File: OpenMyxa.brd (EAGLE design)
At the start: 56 x 56 mm, 107 parts, among them CON1 USB, CON2 PINHEAD_1X01-2, CON3 CON-4P-STRAIGHT, CON4 CON-4P-STRAIGHT, CON5 CON-4P-STRAIGHT, CON6 CON-4P-STRAIGHT, CON7 CON-4P-STRAIGHT, CON8 CON-6P, CON9 PINHEAD_1X01-2, IC1 TPD3S014DBVR-SOT23-6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

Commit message: V0.2 import
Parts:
- removed D3: TPSMC62A, TVS_diodes:DO-214AB(SMC)
- removed MODULE1: MITOHONDRIQUE, mitohondrique:MITOHONDRIQUE
- added MODULE2: MITOHONDRIQUE-TH, zubax_modules:MITOHONDRIQUE
- CON3, CON4, CON5, CON6: device myxa_masterlib:JST_GH-4P-STRAIGHT -> Connectors:JST_GH-4P-STRAIGHT
- moved R7 12.3 mm to (-21.2, 5.90)
- moved PAD6 7.30 mm to (-26.5, -3.65), turned to 270 degrees
- moved PAD7 7.30 mm to (-26.5, 3.65), turned to 270 degrees
- moved U$13 4.69 mm to (-9.28, 18.1)
- moved R10 4.10 mm to (-3.00, 1.25), turned to 90 degrees
- moved LED5 3.76 mm to (-13.3, 18.5), turned to 90 degrees
- moved LED4 3.73 mm to (-10.3, 18.5), turned to 270 degrees
- moved LED3 2.90 mm to (-7.28, 18.5), turned to 270 degrees
- moved R13 2.57 mm to (-9.35, 16.8), flipped to the top
- moved R12 2.30 mm to (-8.30, 16.8), flipped to the top
- moved R11 2.19 mm to (-7.25, 16.8), flipped to the top
- moved CON2 2.00 mm to (-26.5, 1.00), turned to 270 degrees
- moved CON9 2.00 mm to (-26.5, -1.00), turned to 270 degrees
- moved R28 1.67 mm to (-10.2, 22.4)
- moved D7 1.36 mm to (-11.1, 16.5), flipped to the top, turned to 90 degrees
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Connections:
- removed net N$23: CON3.2, CON4.2, IC3.6
- removed net N$24: CON7.2, R25.2
- removed net N$35: CON3.3, CON4.3, IC3.7
- new net LED_BLUE: MODULE2.32, R11.2
- new net N$21: CON3.2, CON4.2, IC3.7
- new net N$22: CON3.3, CON4.3, IC3.6
- net BEC_ENABLE_OUT: now also MODULE2.24; no longer MODULE1.24
- net CAN1_LED: now also MODULE2.36; no longer MODULE1.27
- net CAN1_RX: now also MODULE2.41; no longer MODULE1.41
- net CAN1_TX: now also MODULE2.42; no longer MODULE1.42
- net CAN1_VDD: now also CON3.1, CON4.1; no longer CON3.4, CON4.4
- net CAN2_LED: now also MODULE2.37; no longer MODULE1.26
- net CAN2_RX: now also MODULE2.39; no longer MODULE1.39
- net CAN2_TX: now also MODULE2.40; no longer MODULE1.40
- net CAN2_VDD: now also CON5.1, CON6.1; no longer CON5.4, CON6.4
- net GAIN_OUT: now also MODULE2.25; no longer MODULE1.38
- net GATE_ENABLE_OUT: now also MODULE2.26; no longer MODULE1.37
- net GND: now also CON7.4, MODULE2.2; no longer CON7.1, MODULE1.2
- net GNDD: now also CON3.4, CON4.4, CON5.4, CON6.4; no longer CON3.1, CON4.1, CON5.1, CON6.1
- net GPIO1: now also MODULE2.28; no longer MODULE1.35
- net GPIO2: now also MODULE2.27; no longer MODULE1.36
- net LED_GREEN: now also MODULE2.31; no longer MODULE1.32
- net LED_RED: now also MODULE2.30; no longer MODULE1.33
- net N$18: now also MODULE2.29; no longer MODULE1.34
- net N$19: now also CON7.2, R8.2; no longer CON7.4, F1.P$1
- net N$20: now also R25.2; no longer R8.2
- net N$44: now also CON5.3, CON6.3; no longer CON5.2, CON6.2
- net N$46: now also CON5.2, CON6.2; no longer CON5.3, CON6.3
- net N$5: now also MODULE2.33; no longer MODULE1.30
- net N$51: now also MODULE2.34; no longer MODULE1.29
- net N$55: now also MODULE2.35; no longer MODULE1.28
- net N$6: now also CON7.1, F1.P$1; no longer MODULE1.31, R11.2
- net PGND: no longer D3.A
- net PHASE_A: now also MODULE2.5; no longer MODULE1.5
- net PHASE_A_CURRENT_SHUNT_N: now also MODULE2.16; no longer MODULE1.16
- net PHASE_A_CURRENT_SHUNT_P: now also MODULE2.17; no longer MODULE1.17
- net PHASE_A_GATE_HIGH: now also MODULE2.4; no longer MODULE1.4
- net PHASE_A_GATE_LOW: now also MODULE2.6; no longer MODULE1.6
- net PHASE_A_GND: now also MODULE2.7; no longer MODULE1.7
- net PHASE_B: now also MODULE2.9; no longer MODULE1.9
- net PHASE_B_CURRENT_SHUNT_N: now also MODULE2.18; no longer MODULE1.18
- net PHASE_B_CURRENT_SHUNT_P: now also MODULE2.19; no longer MODULE1.19
- net PHASE_B_GATE_HIGH: now also MODULE2.8; no longer MODULE1.8
- net PHASE_B_GATE_LOW: now also MODULE2.10; no longer MODULE1.10
- net PHASE_B_GND: now also MODULE2.11; no longer MODULE1.11
- net PHASE_C: now also MODULE2.13; no longer MODULE1.13
- net PHASE_C_GATE_HIGH: now also MODULE2.12; no longer MODULE1.12
- net PHASE_C_GATE_LOW: now also MODULE2.14; no longer MODULE1.14
- net PHASE_C_GND: now also MODULE2.15; no longer MODULE1.15
- net TEMPERATURE_SENSOR: now also MODULE2.20; no longer MODULE1.20
- net UART_RX: now also MODULE2.23, R29.2; no longer MODULE1.23, R28.2
- net UART_TX: now also MODULE2.22, R28.2; no longer MODULE1.22, R29.2
- net VDC: now also MODULE2.3; no longer D3.C, MODULE1.3
- net VDD_5V: now also MODULE2.1; no longer MODULE1.1
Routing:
- net GAIN_OUT: track 46.1 -> 15.0 mm
- net LED_BLUE: track 0.00 -> 28.4 mm
- net GATE_ENABLE_OUT: track 45.4 -> 18.6 mm
- net N$6: track 30.7 -> 5.93 mm, vias 1 -> 0
- net GPIO2: track 41.8 -> 17.4 mm
- net GPIO1: track 45.7 -> 29.2 mm
- net CAN1_LED: track 25.5 -> 37.0 mm, vias 0 -> 1
- net N$23: track 11.5 -> 0.00 mm
- net N$22: track 0.00 -> 11.5 mm
- net CAN2_LED: track 39.0 -> 27.8 mm, vias 2 -> 1
- net N$35: track 10.4 -> 0.00 mm
- net N$21: track 0.00 -> 10.4 mm
- net N$55: track 9.44 -> 19.1 mm, vias 0 -> 1
- net LED_RED: track 32.3 -> 23.7 mm, vias 1 -> 0
- net N$5: track 2.09 -> 9.95 mm
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- added copper zone on layer 15, net VDD_5V
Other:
- outline, holes or cut-outs redrawn
- board text added: "OpenMyxa0.2"
- board text removed: "OpenMyxa"

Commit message: minor updates
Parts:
- moved CON2 1.00 mm to (-25.5, 1.00)
- moved CON9 1.00 mm to (-25.5, -1.00)
- moved PAD6 1.00 mm to (-25.5, -3.65)
- moved PAD7 1.00 mm to (-25.5, 3.65)
- moved C32 0.80 mm to (14.2, 21.4)
- moved C35 0.80 mm to (14.2, -21.4)
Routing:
- net GND: track 30.7 -> 33.5 mm

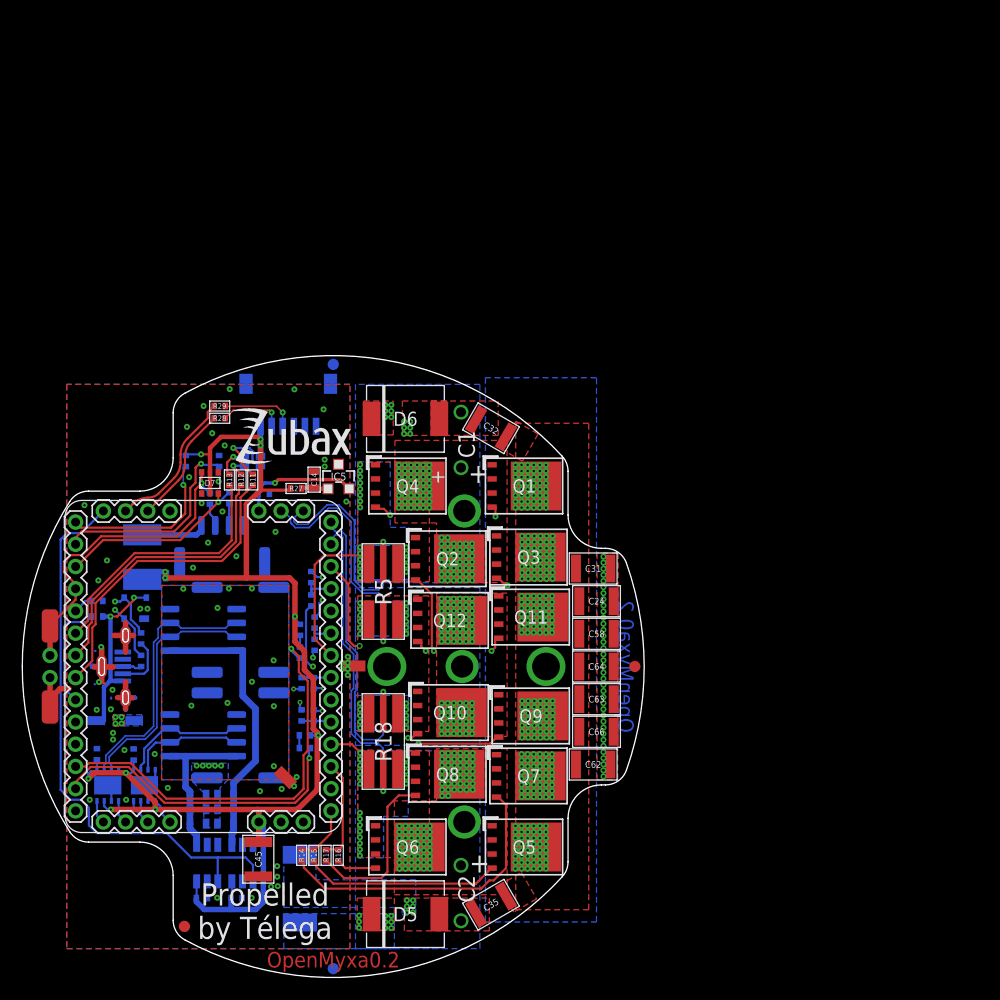
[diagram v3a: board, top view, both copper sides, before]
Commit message: Connectors color fix
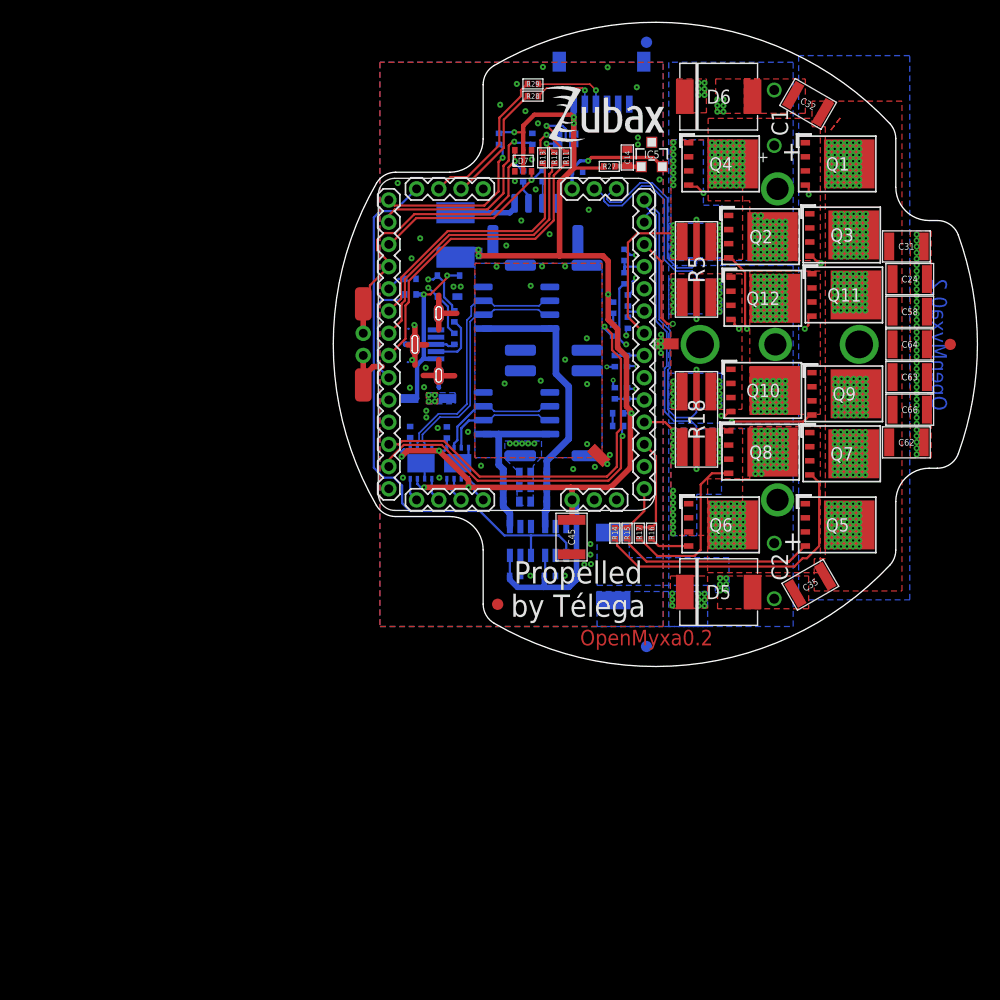
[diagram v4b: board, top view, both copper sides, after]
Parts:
- CON3, CON4, CON5, CON6, CON7: value CON-4P-STRAIGHT -> CON-4P-TABS-STRAIGHT
- MODULE2: device zubax_modules:MITOHONDRIQUE -> zubax_modules:MITOHONDRIQUE-TH
- moved C32 40.8 mm to (42.8, 50.6)
- moved C35 40.7 mm to (43.0, 7.35)
- moved U$5 40.6 mm to (55.5, 29.0)
- moved C1 40.5 mm to (39.2, 49.4)
- moved C12 40.5 mm to (10.2, 21.1)
- moved C13 40.5 mm to (21.9, 44.5)
- moved C14 40.5 mm to (26.5, 45.8)
- moved C2 40.5 mm to (39.2, 8.60)
- moved C24 40.5 mm to (51.9, 34.9)
- moved C31 40.5 mm to (51.6, 37.8)
- moved C62 40.5 mm to (51.6, 20.2)
- moved CON5 40.5 mm to (22.4, 32.3)
- moved CON6 40.5 mm to (16.4, 32.3)
- moved CON7 40.5 mm to (18.2, 38.8)
- moved D5 40.5 mm to (34.7, 6.70)
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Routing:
- net GND: track 33.5 -> 34.9 mm, vias 51 -> 50
- net BEC_ENABLE_OUT: track 52.1 -> 51.4 mm
- net VDD_5V: track 139.7 -> 140.4 mm
- net UART_RX: track 13.1 -> 13.6 mm
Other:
- board size 56 x 56 mm -> 58 x 58 mm
